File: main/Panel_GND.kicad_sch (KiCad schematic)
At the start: 8 parts

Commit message: added logos, oranised sheets, final version
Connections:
- new net: ADS1. (V), ISO1. (VCC) (x2)
- new net: ADS1. (V), NTC1., R3.1
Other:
- company: (none) -> Designers: Krzysztof Grajek, Wojtek Kołodziej

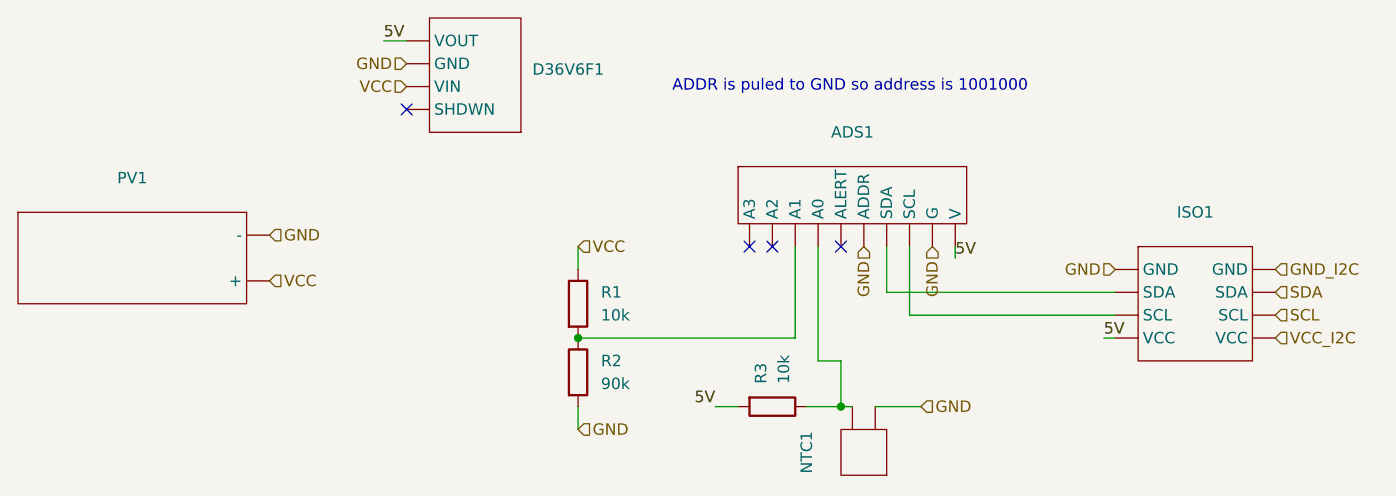
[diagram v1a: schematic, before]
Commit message: Changed name of Adafruit 4903(i2c spearator). Changed values of resistors used in panels
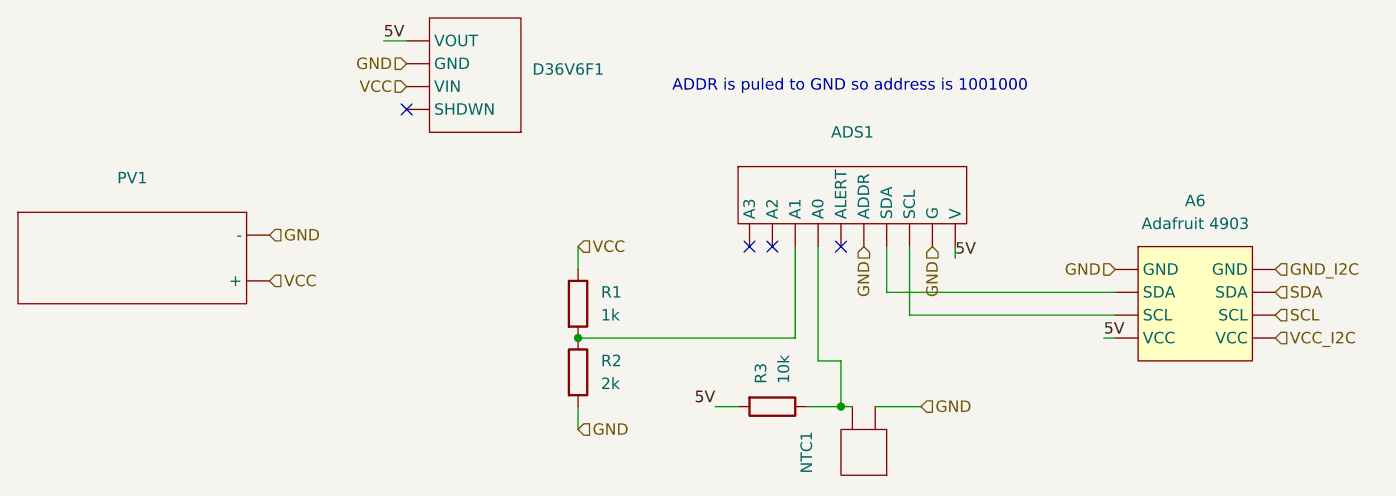
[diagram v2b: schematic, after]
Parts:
- removed ISO1: ~, symbol New_Library_0:Bidirectional I2C Isolator
- added A6: Adafruit 4903, symbol New_Library_0:Adafruit_4903
- R1: value 10k -> 1k
- R2: value 90k -> 2k
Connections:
- net 5V: now also A6. (VCC)
- net GND: now also A6. (VCC)
- net GND_I2C: now also A6. (VCC)
- net SCL: now also A6. (VCC)
- net SDA: now also A6. (VCC)
- net VCC_I2C: now also A6. (VCC)
- new net: A6. (VCC), ADS1. (V) (x2)
- new net: ADS1. (V), NTC1., R3.1
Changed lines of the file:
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@@
 	)
 	(symbol
-		(lib_id "New_Library_0:Bidirectional I2C Isolator")
+		(lib_id "New_Library_0:Adafruit_4903")
 		(at 170.18 81.28 0)
 		(unit 1)
@@
 		(dnp no)
 		(fields_autoplaced yes)
-		(property "Reference" "ISO1"
-			(at 170.18 71.12 0)
-			(effects
-				(font
-					(size 1.27 1.27)
-				)
-			)
-		)
-		(property "Value" "~"
-			(at 170.18 73.66 0)
+		(property "Reference" "A6"
+			(at 170.18 69.85 0)
+			(effects
+				(font
+					(size 1.27 1.27)
+				)
+			)
+		)
+		(property "Value" "Adafruit 4903"
+			(at 170.18 72.39 0)
 			(effects
 				(font
@@
 			(project "main"
 				(path "/54fbbba9-a737-4199-9a4b-f9fa49b3de5e/42b38d5d-5c36-4712-95e4-9fdfab477064/1aa19d72-d0bb-4270-af3b-82323521a6b0"
-					(reference "ISO1")
+					(reference "A6")
 					(unit 1)
 				)
 				(path "/54fbbba9-a737-4199-9a4b-f9fa49b3de5e/42b38d5d-5c36-4712-95e4-9fdfab477064/2d1bd2db-8199-4386-8baa-2410ff23ec16"
-					(reference "ISO8")
+					(reference "A13")
 					(unit 1)
 				)
 				(path "/54fbbba9-a737-4199-9a4b-f9fa49b3de5e/42b38d5d-5c36-4712-95e4-9fdfab477064/33cd4aa0-f224-4e64-b167-bf49e33bde75"
-					(reference "ISO5")
+					(reference "A10")
 					(unit 1)
 				)
 				(path "/54fbbba9-a737-4199-9a4b-f9fa49b3de5e/42b38d5d-5c36-4712-95e4-9fdfab477064/49f3f52e-02cd-4475-a3fa-c9e5c914d4da"
-					(reference "ISO3")
+					(reference "A8")
 					(unit 1)
 				)
 				(path "/54fbbba9-a737-4199-9a4b-f9fa49b3de5e/42b38d5d-5c36-4712-95e4-9fdfab477064/53b34285-37f0-4b71-a456-cfca14ce7f77"
-					(reference "ISO6")
+					(reference "A11")
 					(unit 1)
 				)
 				(path "/54fbbba9-a737-4199-9a4b-f9fa49b3de5e/42b38d5d-5c36-4712-95e4-9fdfab477064/62add4f6-fcf5-4a4e-a16c-e46d7e282ca1"
-					(reference "ISO4")
+					(reference "A9")
 					(unit 1)
 				)
 				(path "/54fbbba9-a737-4199-9a4b-f9fa49b3de5e/42b38d5d-5c36-4712-95e4-9fdfab477064/9c45c600-1aba-4c76-a275-afa6e0cdd76b"
-					(reference "ISO2")
+					(reference "A7")
 					(unit 1)
 				)
 				(path "/54fbbba9-a737-4199-9a4b-f9fa49b3de5e/42b38d5d-5c36-4712-95e4-9fdfab477064/a29e76b4-4efd-4022-9cbf-018c9a0b5ec8"
-					(reference "ISO7")
+					(reference "A12")
 					(unit 1)
 				)
@@
 			)
 		)
-		(property "Value" "90k"
+		(property "Value" "2k"
 			(at 104.14 90.1699 0)
 			(effects
@@
 			)
 		)
-		(property "Value" "10k"
+		(property "Value" "1k"
 			(at 104.14 82.5499 0)
 			(effects
